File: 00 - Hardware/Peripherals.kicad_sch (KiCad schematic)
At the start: 12 parts, among them J1 Conn_01x04_Pin, J3 Conn_01x04_Pin, J6 Conn_01x04_Pin, U6 FT231XS

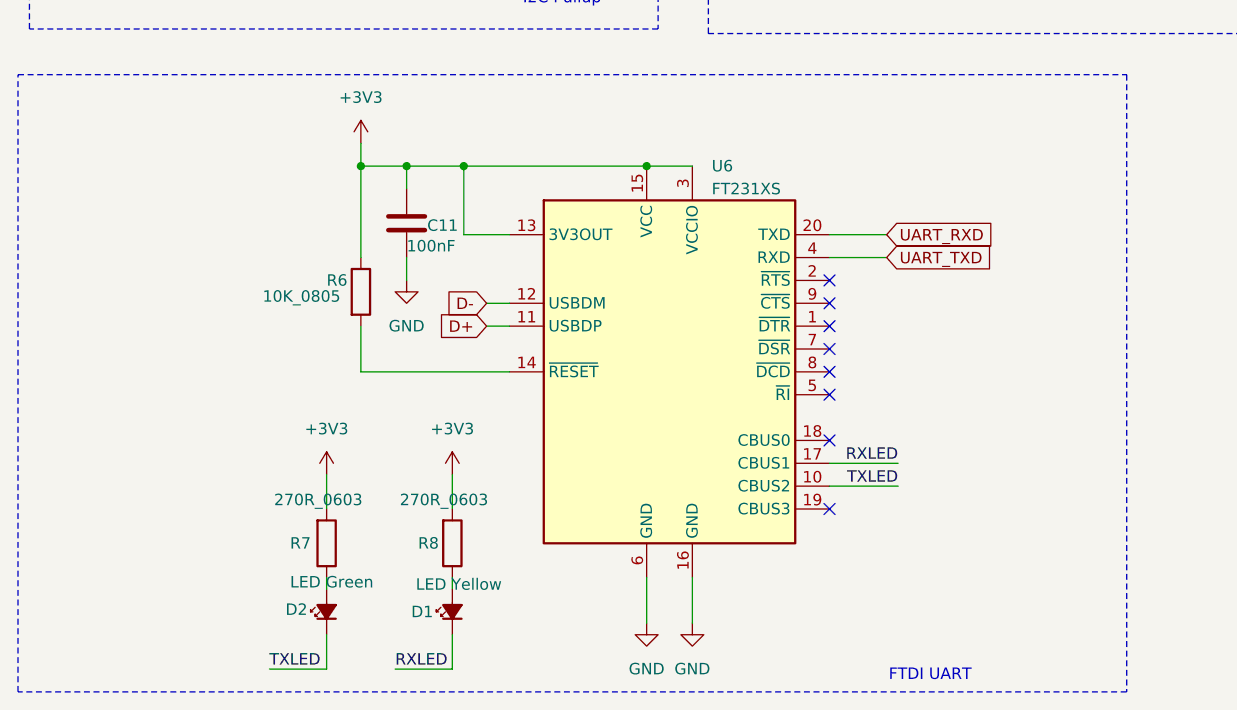
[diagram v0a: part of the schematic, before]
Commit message: updated FDTI cbus connections
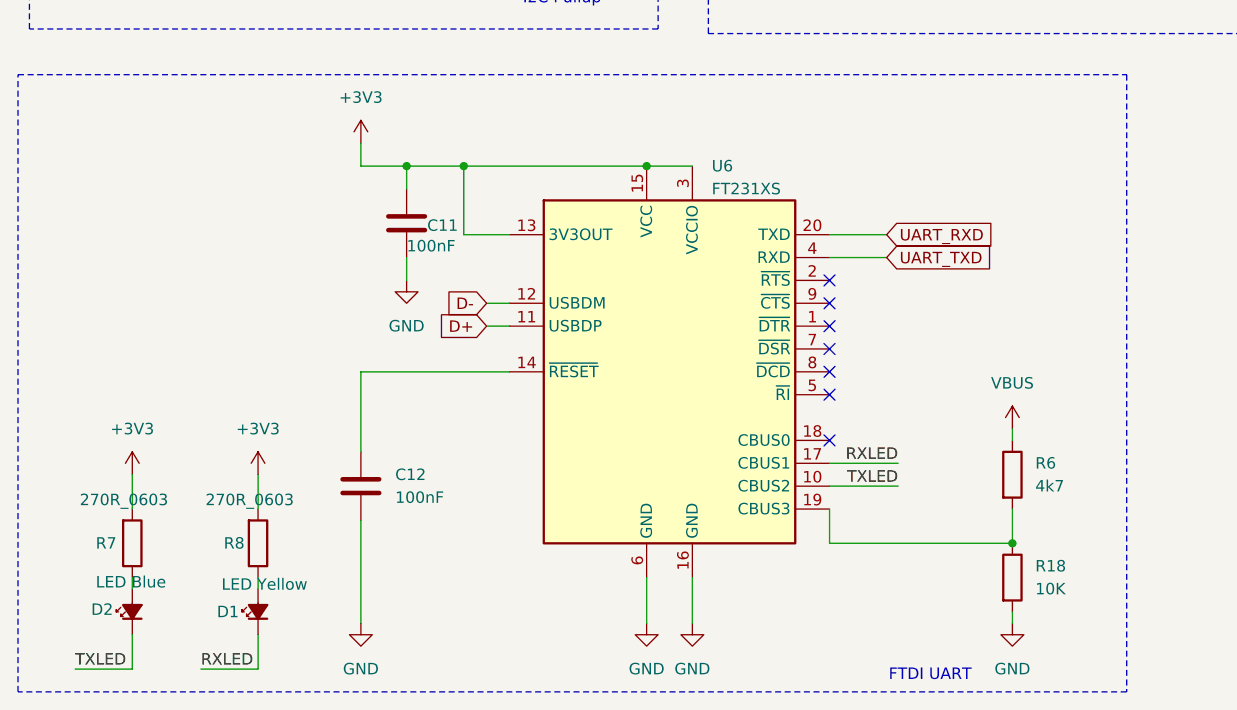
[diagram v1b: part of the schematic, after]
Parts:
- removed R6: 10K_0805, Project_Footprints:R_0805_2012Metric, symbol Library:10K_0805
- added C12: 100nF, Capacitor_SMD:C_0603_1608Metric, symbol Device:C
- added R18: 10K, Resistor_SMD:R_0603_1608Metric, symbol Device:R
- added R6: 4k7, Resistor_SMD:R_0603_1608Metric, symbol Device:R
- D1: MPN1 APTD2012LCGCK -> APTD2012LSYCK
- D2: value LED Green -> LED Blue; MPN1 APTD2012LCGCK -> APTD2012LQBC/D
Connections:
- net GND: now also C12.2, R18.2
- net at U6.14 (~{RESET}): now also C12.1
- net at U6.19 (CBUS3): now also R18.1, R6.2
- new net VBUS: R6.1
- no-connect marks 8 -> 7
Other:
- moved on the sheet: D1, D2, R7, R8
